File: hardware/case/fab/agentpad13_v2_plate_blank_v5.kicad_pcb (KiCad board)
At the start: 2 copper layers, 84.4 x 100.2 mm, 0 parts

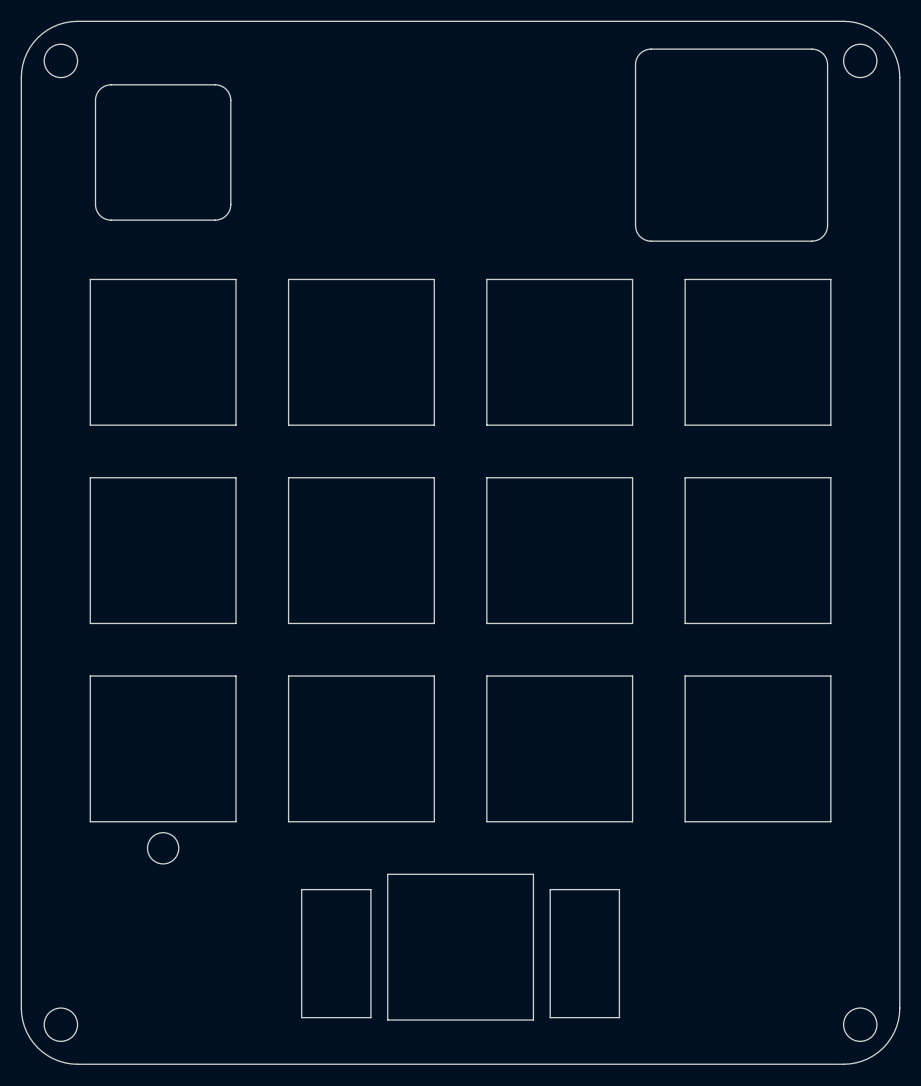
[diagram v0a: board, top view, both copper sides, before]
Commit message: Plate fab set was PRE-TRIM: 100.2 mm long axis, outside the <=100 mm promo tier
The mirror was shipping the plate as it existed BEFORE the owner's 2026-07-21
long-axis trim. Measured from Edge.Cuts on every copy here:

  agentpad13_v2_plate_v5.kicad_pcb              84.400 x 100.200  -> 84.400 x 100.000
  agentpad13_v2_plate_tented_ring_v5.kicad_pcb  84.400 x 100.200  -> 84.400 x 100.000
  agentpad13_v2_plate_blank_v5.kicad_pcb        84.400 x 100.200  -> 84.400 x 100.000
  plate_v5_gerbers.zip (Edge_Cuts.gm1)          84.400 x 100.200  -> 84.400 x 100.000
  plate_v5_ring_gerbers.zip                     84.400 x 100.200  -> 84.400 x 100.000
  plate_v5_blank_gerbers.zip                    84.400 x 100.200  -> 84.400 x 100.000

100.2 mm falls outside the <=100 mm promo tier that PCBWay/JLCPCB price bare
boards on, so anyone ordering a plate from these files paid a materially higher
quote for 0.2 mm of FR4 they never wanted. The trim exists precisely to avoid
that ("Resize the top plates to 100mm. That 0.2 is gonna cost us 25%.") and is
implemented as PLATE_LONG_TRIM = 0.2 in the upstream gen_plate_fab.py: 0.1 mm
off each long edge, outline centred on the same axis.

All nine plate artifacts (3 .kicad_pcb + 3 gerber zips + DXF + PNG + SVG) are
re-synced from the trimmed upstream working tree and are now byte-identical to
it. The change is outline-only: an unordered, UUID-blind set-difference of the
old vs new .kicad_pcb returns exactly 8 changed primitives (the 4 outline edges
and 4 corner arcs) out of 93 -- every switch cutout, the encoder and joystick
openings, the touch/LED holes and all four M3 screw holes keep their exact
absolute positions. Post-trim geometry gates pass on all three variants
(Edge.Cuts shapes 89, joystick opening W58.91/N2.57/E77.36/S21.02, NE->screw
web 1.555 over the 1.5 floor).

Docs:

- HOW-TO-ORDER.md gasket stock 1-2 mm -> 0.5 mm. The kit's own README sizes the
  segments for ~40% compression into the band's 0.3 mm ledge gap; 1-2 mm stock
 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
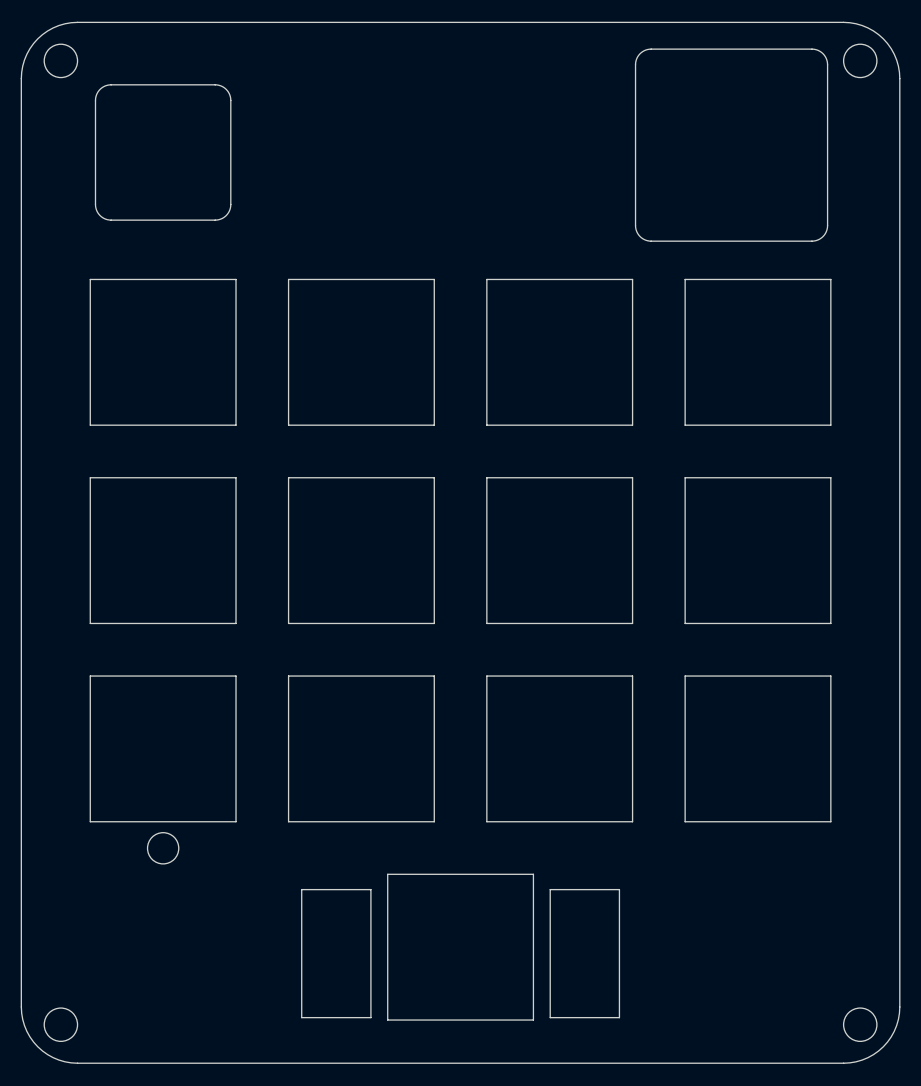
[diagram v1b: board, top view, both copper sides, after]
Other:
- board size 84.4 x 100.2 mm -> 84.4 x 100 mm
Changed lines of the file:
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@@
   (setup (pad_to_mask_clearance 0))
   (net 0 "")
-  (gr_line (start 5.3 -0.1) (end 78.9 -0.1) (stroke (width 0.1) (type solid)) (layer "Edge.Cuts"))
-  (gr_arc (start 84.3 5.3) (mid 82.7184 1.4816) (end 78.9 -0.1) (stroke (width 0.1) (type solid)) (layer "Edge.Cuts"))
-  (gr_line (start 84.3 5.3) (end 84.3 94.7) (stroke (width 0.1) (type solid)) (layer "Edge.Cuts"))
-  (gr_arc (start 78.9 100.1) (mid 82.7184 98.5184) (end 84.3 94.7) (stroke (width 0.1) (type solid)) (layer "Edge.Cuts"))
-  (gr_line (start 78.9 100.1) (end 5.3 100.1) (stroke (width 0.1) (type solid)) (layer "Edge.Cuts"))
-  (gr_arc (start -0.1 94.7) (mid 1.4816 98.5184) (end 5.3 100.1) (stroke (width 0.1) (type solid)) (layer "Edge.Cuts"))
-  (gr_line (start -0.1 94.7) (end -0.1 5.3) (stroke (width 0.1) (type solid)) (layer "Edge.Cuts"))
-  (gr_arc (start 5.3 -0.1) (mid 1.4816 1.4816) (end -0.1 5.3) (stroke (width 0.1) (type solid)) (layer "Edge.Cuts"))
+  (gr_line (start 5.3 0) (end 78.9 0) (stroke (width 0.1) (type solid)) (layer "Edge.Cuts"))
+  (gr_arc (start 84.3 5.4) (mid 82.7184 1.5816) (end 78.9 0) (stroke (width 0.1) (type solid)) (layer "Edge.Cuts"))
+  (gr_line (start 84.3 5.4) (end 84.3 94.6) (stroke (width 0.1) (type solid)) (layer "Edge.Cuts"))
+  (gr_arc (start 78.9 100) (mid 82.7184 98.4184) (end 84.3 94.6) (stroke (width 0.1) (type solid)) (layer "Edge.Cuts"))
+  (gr_line (start 78.9 100) (end 5.3 100) (stroke (width 0.1) (type solid)) (layer "Edge.Cuts"))
+  (gr_arc (start -0.1 94.6) (mid 1.4816 98.4184) (end 5.3 100) (stroke (width 0.1) (type solid)) (layer "Edge.Cuts"))
+  (gr_line (start -0.1 94.6) (end -0.1 5.4) (stroke (width 0.1) (type solid)) (layer "Edge.Cuts"))
+  (gr_arc (start 5.3 0) (mid 1.4816 1.5816) (end -0.1 5.4) (stroke (width 0.1) (type solid)) (layer "Edge.Cuts"))
   (gr_line (start 6.525 24.7) (end 20.525 24.7) (stroke (width 0.1) (type solid)) (layer "Edge.Cuts"))
   (gr_line (start 20.525 24.7) (end 20.525 38.7) (stroke (width 0.1) (type solid)) (layer "Edge.Cuts"))

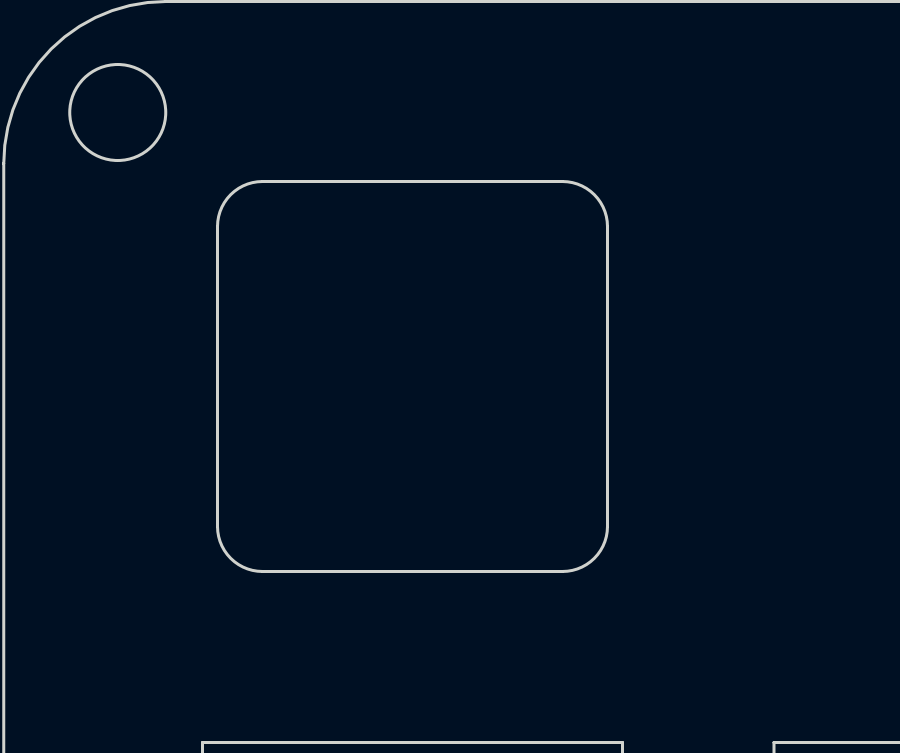
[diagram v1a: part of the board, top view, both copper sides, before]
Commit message: Case: the encoder didn't fit the plate, and the tray was mirrored
Two separate defects in the published case files, both of which cost you a
part if you built from them.

The plate's encoder aperture was 13.0 x 13.0 mm, centred on the shaft. Common
EC11 encoders are not that small: the ones this build was validated against
measure about 13.7 mm across the pin axis, and the body fouled one wall of the
opening on assembly -- it seated fine on one side and bound on the other. The
opening is now 14.0 x 13.0 mm. The extra 1.0 mm went entirely onto the side
that bound; the opposite edge did not move, so the shaft now sits 0.5 mm off
the aperture centre by design. Corner radius stays 1.5 mm, deliberately --
enlarging it would eat the very corner clearance a larger body needs.

That has one cosmetic cost, and it is accepted rather than fixed: the two
widened corners now reach 9.31 mm from the shaft, so the 18 mm knurled_cup
knob (radius 9.0) leaves roughly 0.3 mm of the opening visible at each of
them. Print the 19 mm dome_cup if it bothers you -- it covers completely.
Separately, ribbed_skirt's internal relief cavity was sized for an 11.7 mm
encoder body and has not been verified against the larger ones; if yours is a
big one, use knurled_cup or dome_cup. Both notes are in the case README.

The tray published here was several revisions behind and was mirror-imaged --
a printed copy came out the wrong hand, and its locating posts did not line up
with the board. Two more faults went with it: a continuous lip around the PCB
edge that stood directly in front of the ten side-firing underglow LEDs, and a
stray square hole through the floor near the encoder corner (a boss-relief
cutter that was never bounded). The current tray fixes all three -- the lip is
now fourteen short support columns that leave the light path open -- and adds
four 6 mm base pockets in the underside on a 25 mm square for optional printed
bases, plus a 2.0 mm plinth: the tray now stands slightly proud below 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
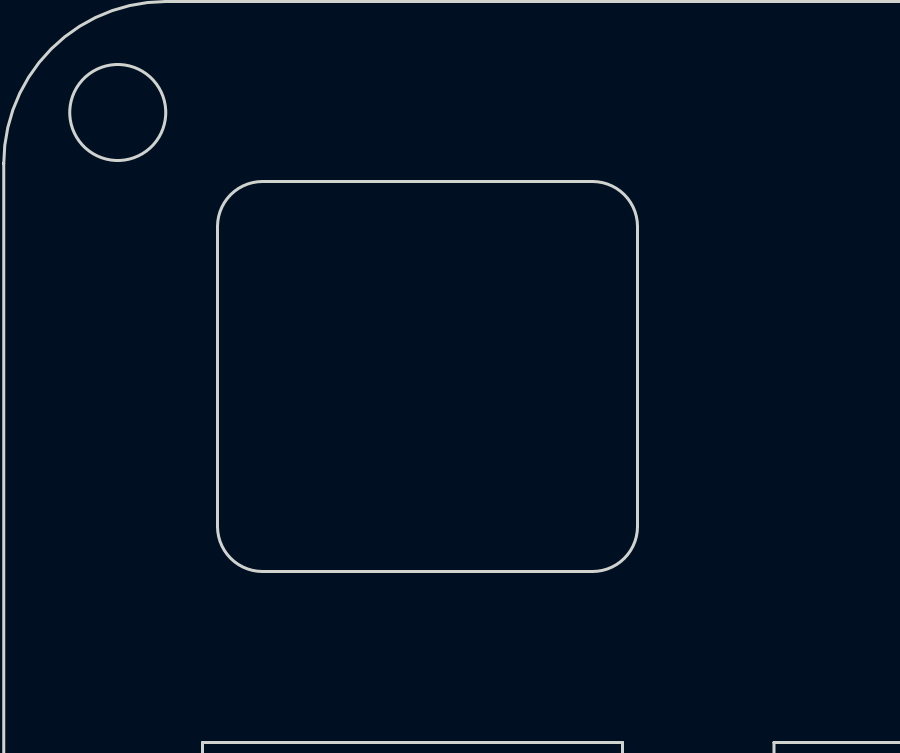
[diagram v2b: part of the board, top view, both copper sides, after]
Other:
- outline, holes or cut-outs redrawn
- board text added: "WayWayWay"
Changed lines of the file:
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@@
   (gr_line (start 57.363 95.62) (end 50.713 95.62) (stroke (width 0.1) (type solid)) (layer "Edge.Cuts"))
   (gr_line (start 50.713 95.62) (end 50.713 83.32) (stroke (width 0.1) (type solid)) (layer "Edge.Cuts"))
-  (gr_line (start 8.525 6) (end 18.525 6) (stroke (width 0.1) (type solid)) (layer "Edge.Cuts"))
-  (gr_arc (start 20.025 7.5) (mid 19.5857 6.4393) (end 18.525 6) (stroke (width 0.1) (type solid)) (layer "Edge.Cuts"))
-  (gr_line (start 20.025 7.5) (end 20.025 17.5) (stroke (width 0.1) (type solid)) (layer "Edge.Cuts"))
-  (gr_arc (start 18.525 19) (mid 19.5857 18.5607) (end 20.025 17.5) (stroke (width 0.1) (type solid)) (layer "Edge.Cuts"))
-  (gr_line (start 18.525 19) (end 8.525 19) (stroke (width 0.1) (type solid)) (layer "Edge.Cuts"))
+  (gr_line (start 8.525 6) (end 19.525 6) (stroke (width 0.1) (type solid)) (layer "Edge.Cuts"))
+  (gr_arc (start 21.025 7.5) (mid 20.5857 6.4393) (end 19.525 6) (stroke (width 0.1) (type solid)) (layer "Edge.Cuts"))
+  (gr_line (start 21.025 7.5) (end 21.025 17.5) (stroke (width 0.1) (type solid)) (layer "Edge.Cuts"))
+  (gr_arc (start 19.525 19) (mid 20.5857 18.5607) (end 21.025 17.5) (stroke (width 0.1) (type solid)) (layer "Edge.Cuts"))
+  (gr_line (start 19.525 19) (end 8.525 19) (stroke (width 0.1) (type solid)) (layer "Edge.Cuts"))
   (gr_arc (start 7.025 17.5) (mid 7.4643 18.5607) (end 8.525 19) (stroke (width 0.1) (type solid)) (layer "Edge.Cuts"))
   (gr_line (start 7.025 17.5) (end 7.025 7.5) (stroke (width 0.1) (type solid)) (layer "Edge.Cuts"))
@@
   (gr_circle (center 3.7 96.3) (end 5.3 96.3) (stroke (width 0.1) (type solid)) (fill no) (layer "Edge.Cuts"))
   (gr_circle (center 80.5 96.3) (end 82.1 96.3) (stroke (width 0.1) (type solid)) (fill no) (layer "Edge.Cuts"))
+  (gr_text "WayWayWay" (at 42.1 41.225 0) (layer "B.SilkS") (effects (font (size 1.5 1.5) (thickness 0.225)) (justify mirror)))
 )
